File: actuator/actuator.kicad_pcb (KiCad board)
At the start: 2 copper layers, 31.7 x 90.2 mm, 37 parts, among them J1 Conn_01x12, J2 Conn_01x40_Socket, U1 HV509, U2 HV509, U3 DRV2665

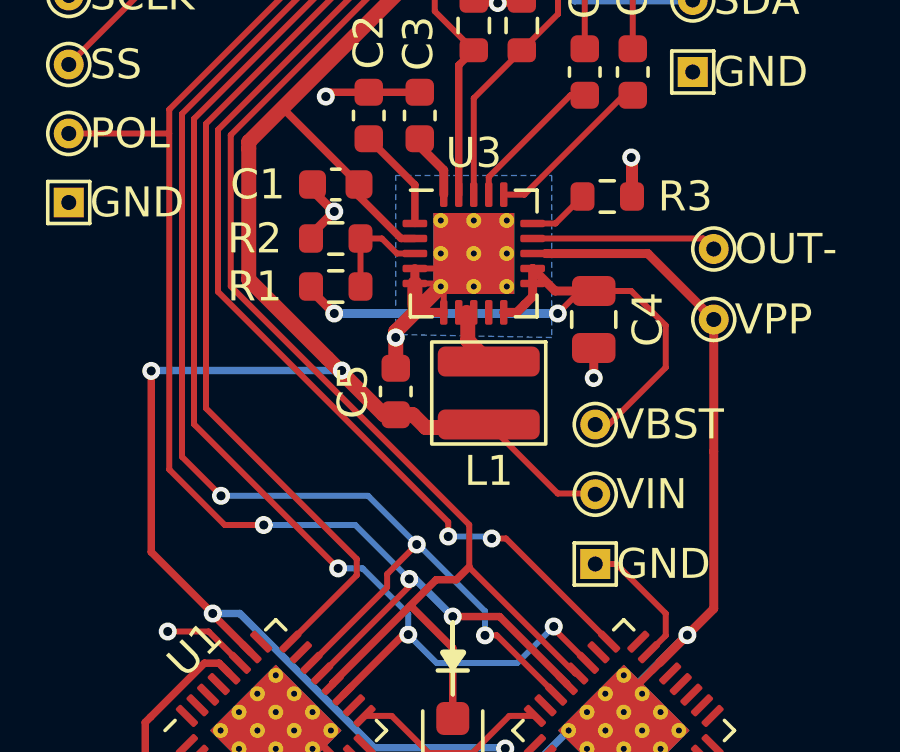
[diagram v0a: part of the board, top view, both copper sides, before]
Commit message: actuator: add capacitor for vdd, no exposed copper on backside
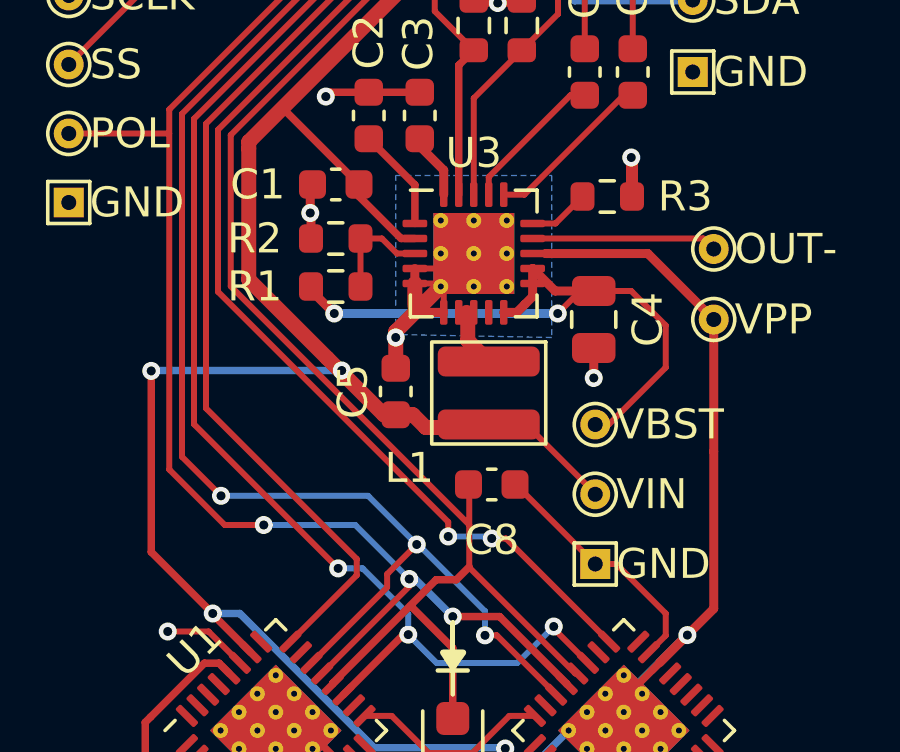
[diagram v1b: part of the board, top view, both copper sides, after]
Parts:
- added C8: 0.1, Capacitor_SMD:C_0603_1608Metric, F.Cu at (105.5, 65.8)
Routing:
- net GND: track 35.1 -> 38.2 mm
- net /VDD: track 65.2 -> 66.5 mm

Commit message: actuator ibom
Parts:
- C8: value 0.1 -> 0.1 µF
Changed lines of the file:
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@@
         (effects (font (size 1 1) (thickness 0.15)))
     )
-    (fp_text value "0.1" (at 0 1.43) (layer "F.Fab")
+    (fp_text value "0.1 µF" (at 0 1.43) (layer "F.Fab")
         (effects (font (size 1 1) (thickness 0.15)))
     )

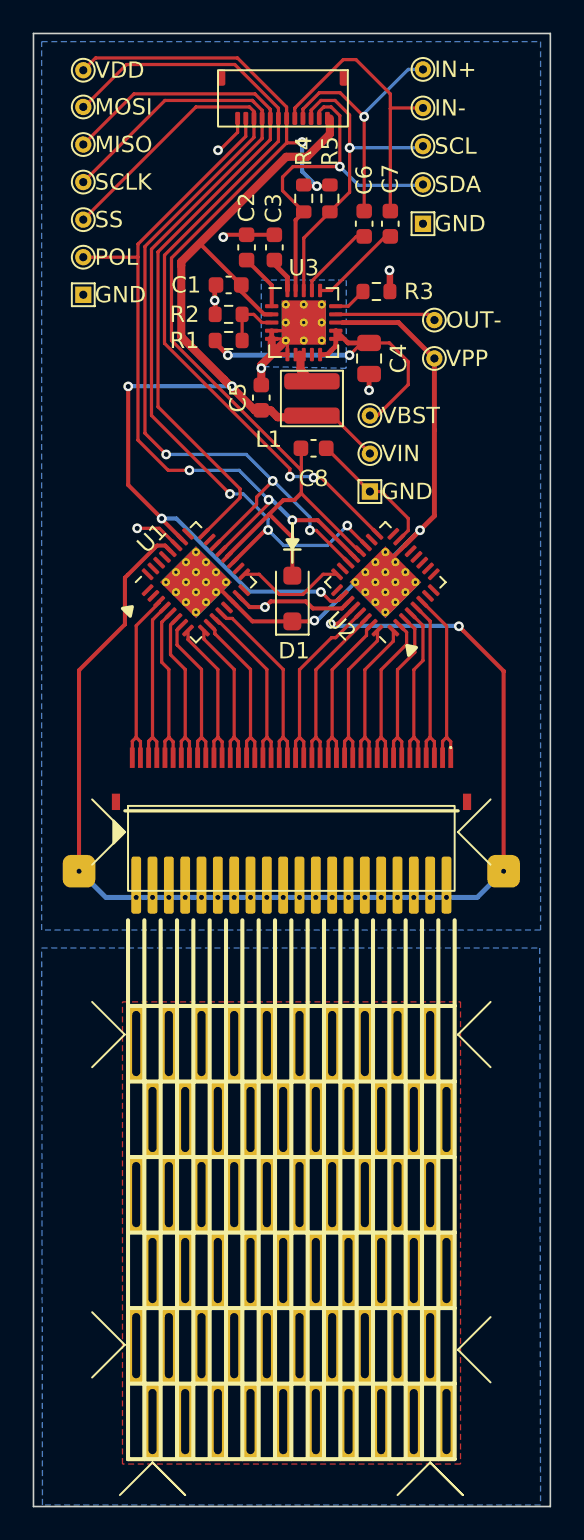
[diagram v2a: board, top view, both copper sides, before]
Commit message: move piezo smd connector, rework pads & adhesive
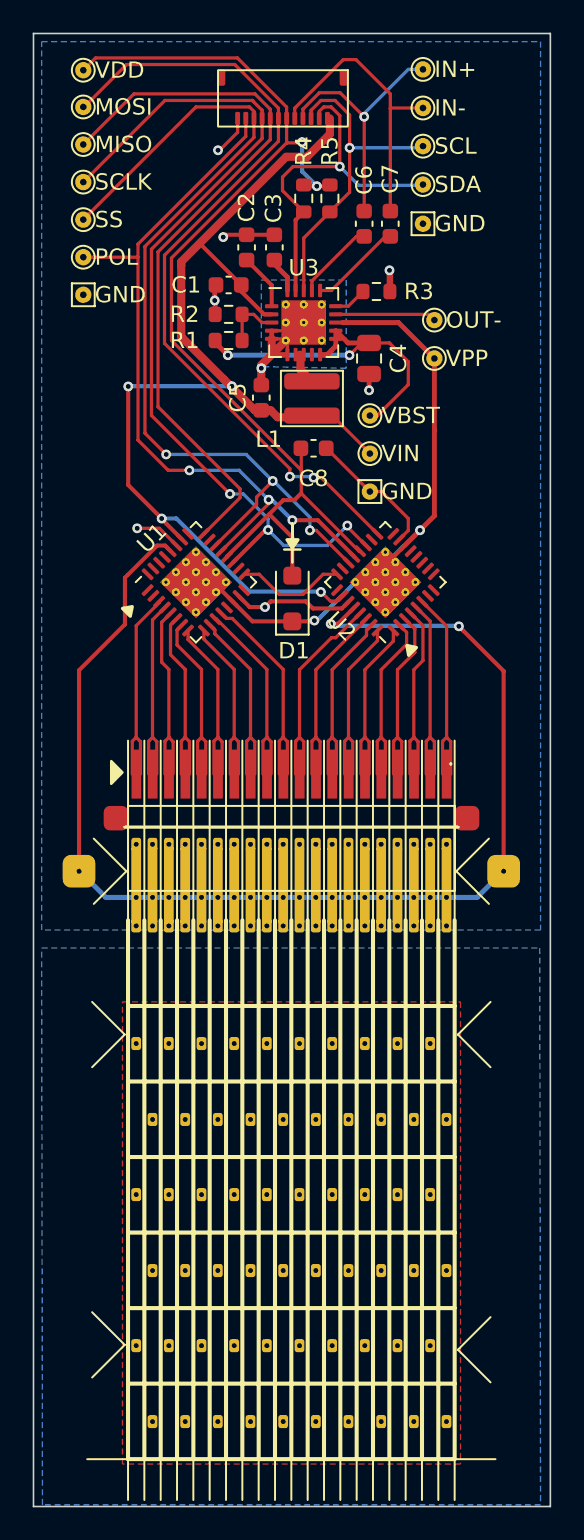
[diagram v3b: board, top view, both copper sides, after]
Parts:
- moved J2 1.00 mm to (104.2, 87.5)
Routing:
- net /reed5: track 10.4 -> 12.4 mm
- net /reed3: track 10.7 -> 12.7 mm
- net /reed11: track 12.0 -> 14.0 mm
- net /reed9: track 11.3 -> 13.3 mm
- net /reed8: track 10.6 -> 12.6 mm
- net /reed7: track 10.0 -> 12.0 mm
- net /reed6: track 10.0 -> 12.0 mm
- net /reed4: track 10.5 -> 12.5 mm
- net /reed20: track 11.6 -> 13.6 mm
- net /reed2: track 11.0 -> 13.0 mm
- net /reed19: track 11.0 -> 13.0 mm
- net /reed18: track 10.9 -> 12.9 mm
- net /reed17: track 10.6 -> 12.6 mm
- net /reed16: track 10.4 -> 12.4 mm
- net /reed15: track 9.97 -> 12.0 mm
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
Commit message: rev3.1 gerbers
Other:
- board text added: "piezo driver board rev 3.1"
- board text removed: "piezo driver board rev 3"
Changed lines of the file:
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@@
     (effects (font (size 1 1) (thickness 0.15)) (justify mirror))
   )
-  (gr_text "piezo driver board\nrev 3" (at 103.95 43.75) (layer "B.SilkS")
+  (gr_text "piezo driver board\nrev 3.1" (at 103.95 43.75) (layer "B.SilkS")
     (effects (font (size 1 1) (thickness 0.15)) (justify mirror))
   )

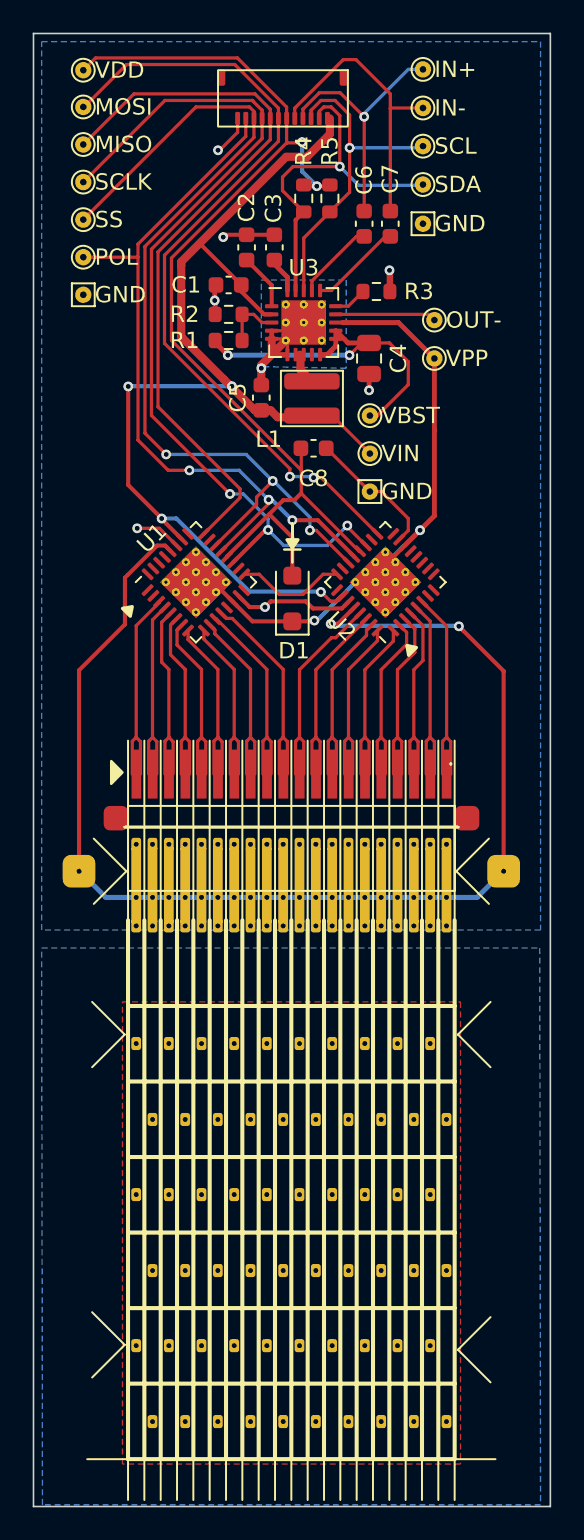
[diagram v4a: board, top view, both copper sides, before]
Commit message: move up ffc connector (fix #1)
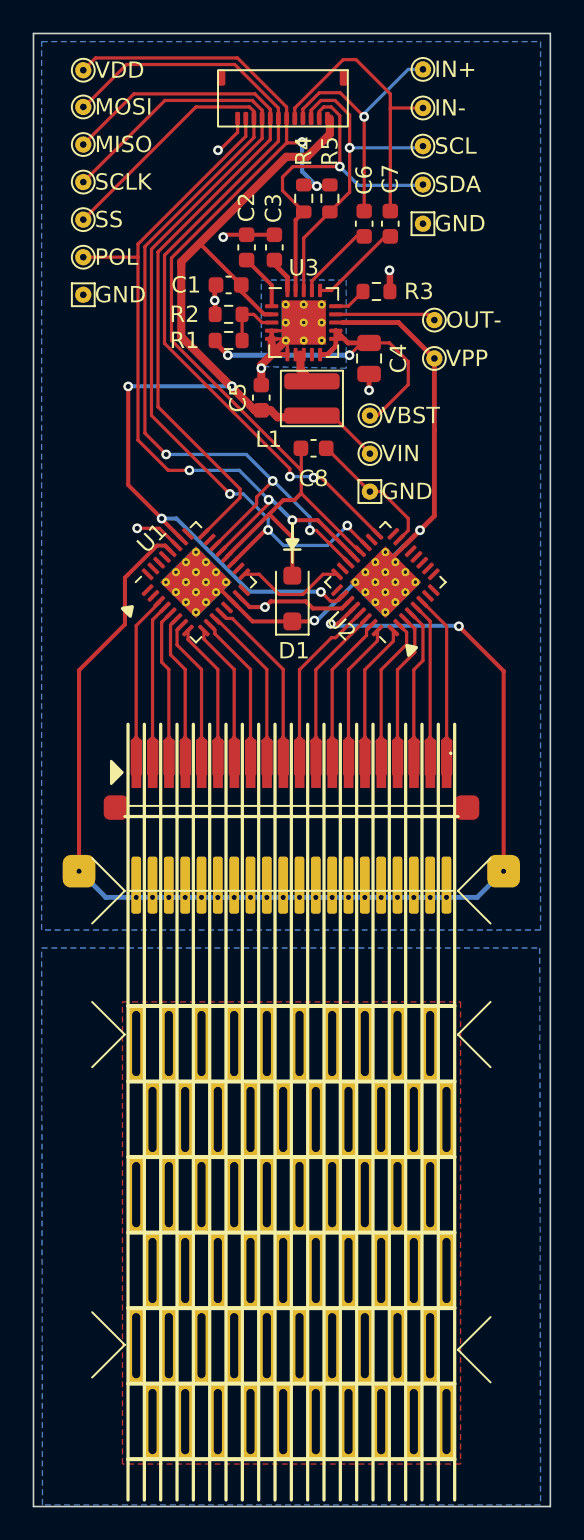
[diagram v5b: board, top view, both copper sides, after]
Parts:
- moved J2 0.65 mm to (104.2, 86.9)

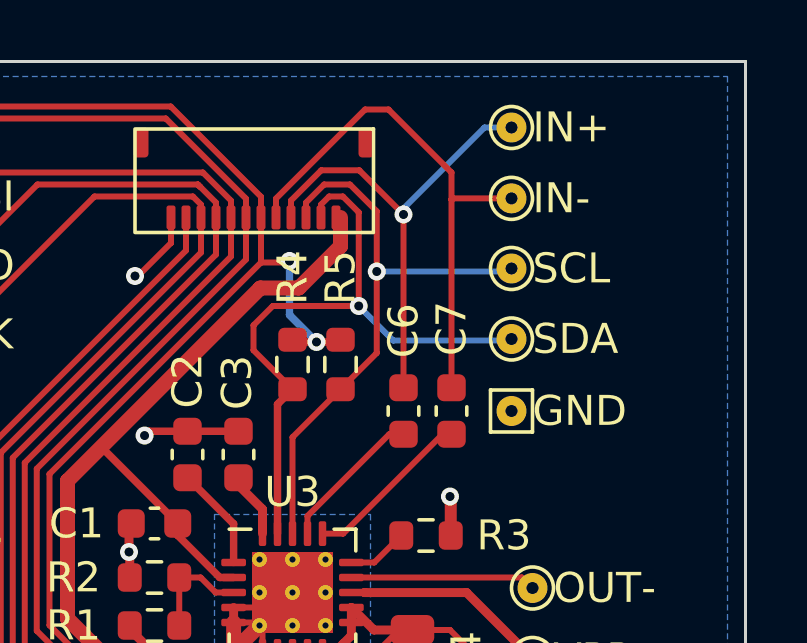
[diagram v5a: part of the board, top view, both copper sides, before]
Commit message: actuator move testpoints to subsheets
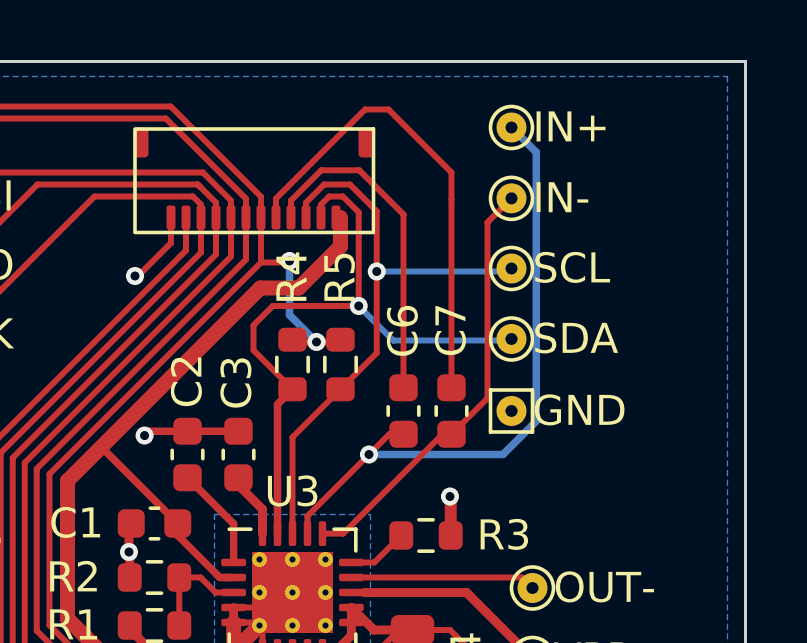
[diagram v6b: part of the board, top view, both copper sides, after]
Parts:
- C6, C7: value 1 µF -> 0.1 µF
- turned C7 to -90 degrees
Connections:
- C7 pad 1: Net-(U3-IN-) -> /IN-
- C7 pad 2: /IN- -> Net-(U3-IN-)
- TP6 pad 1: /IN+ -> Net-(U3-IN+)
- TP7 pad 1: /IN- -> Net-(U3-IN-)
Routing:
- net Net-(U3-IN+): track 4.92 -> 21.1 mm, vias 0 -> 1
- net Net-(U3-IN-): track 5.67 -> 14.4 mm
- net /IN+: track 16.0 -> 11.1 mm, vias 1 -> 0
- net /IN-: track 17.8 -> 15.8 mm

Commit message: add/update revision texts
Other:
- board text added: "piezo driver board rev 3.2"
- board text removed: "piezo driver board rev 3.1"
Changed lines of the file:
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@@
     (effects (font (size 1 1) (thickness 0.15)) (justify mirror))
   )
-  (gr_text "piezo driver board\nrev 3.1" (at 103.95 43.75) (layer "B.SilkS")
+  (gr_text "piezo driver board\nrev 3.2" (at 103.95 43.75) (layer "B.SilkS")
     (effects (font (size 1 1) (thickness 0.15)) (justify mirror))
   )
